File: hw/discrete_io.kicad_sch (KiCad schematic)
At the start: 32 parts, among them Q1 100V logic-level N-ch, Q2 100V logic-level N-ch

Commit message: Draw the connector; the power ground turns out to have no pin
Sheet 10 of 10. Not a circuit -- the harness boundary, and its job is to
be checkable against the machine: every pin the wiring diagram shows
wired to the net whichever sheet owns that signal already named, and
every pin it does not show left visibly empty.

41 of 94 pins wired, 53 left empty, every pin accounted for exactly once
in the netlist.

THE FINDING. GP3.8703.C4.pdf shows pin 21 as the battery positive feed
and shows no battery negative anywhere on the ECU connector. That is a
gap in the source rather than a contradiction in it -- the document is a
field troubleshooting diagram and its own scope note says it omits
"power grounds, unused pins and internal-only pins". It is still a gap
that stops a board: every other sheet in this project returns to GND,
the injector low sides carry 18 A into it, and at this boundary that net
has nowhere to go. It cannot be closed by choosing. Fifty pins have no
established function and several are certainly grounds -- a 94-way
connector feeding an 18 A injector stage does not have one return -- but
a wrong ground pin is not a rework, it is a harness that has to be
remade. Same for TRIP_LOOP, which is a NEW signal not on the OEM diagram
at all and needs one of the same fifty.

CONN_ECU_94 carries pin count and pin numbers, which are facts read off
page 4, and no footprint, because no part number is known. Pin names are
the diagram's own signal names where it shows the pin and blank where it
does not. Same treatment the op-amps and the comparator get.

Two distinctions the sheet makes explicit: pins 34 and 36 are SHARED
sensor returns and therefore signals, carried into difference amplifiers
on sensors_analog; pin 08 is rail pressure's dedicated return, with
nothing to reject, so it is simply ground here.

CROSS-SHEET AUDIT. 83 hierarchical net names across the ten sheets, 73
appearing on two or more. All ten that appear on only one sheet are
explained by an open it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
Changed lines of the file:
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@@
   )
   (hierarchical_label "RLY_MAIN" (shape input) (at 91.68 280.92 180)
-    (effects (font (size 1.27 1.27)) (justify left))
+    (effects (font (size 1.27 1.27)) (justify right))
   )
   (symbol (lib_id "Device:R") (at 101.84 296.92 0) (unit 1)
@@
   )
   (hierarchical_label "RLY_BUZZER" (shape input) (at 291.68 280.92 180)
-    (effects (font (size 1.27 1.27)) (justify left))
+    (effects (font (size 1.27 1.27)) (justify right))
   )
   (symbol (lib_id "Device:R") (at 301.84 296.92 0) (unit 1)

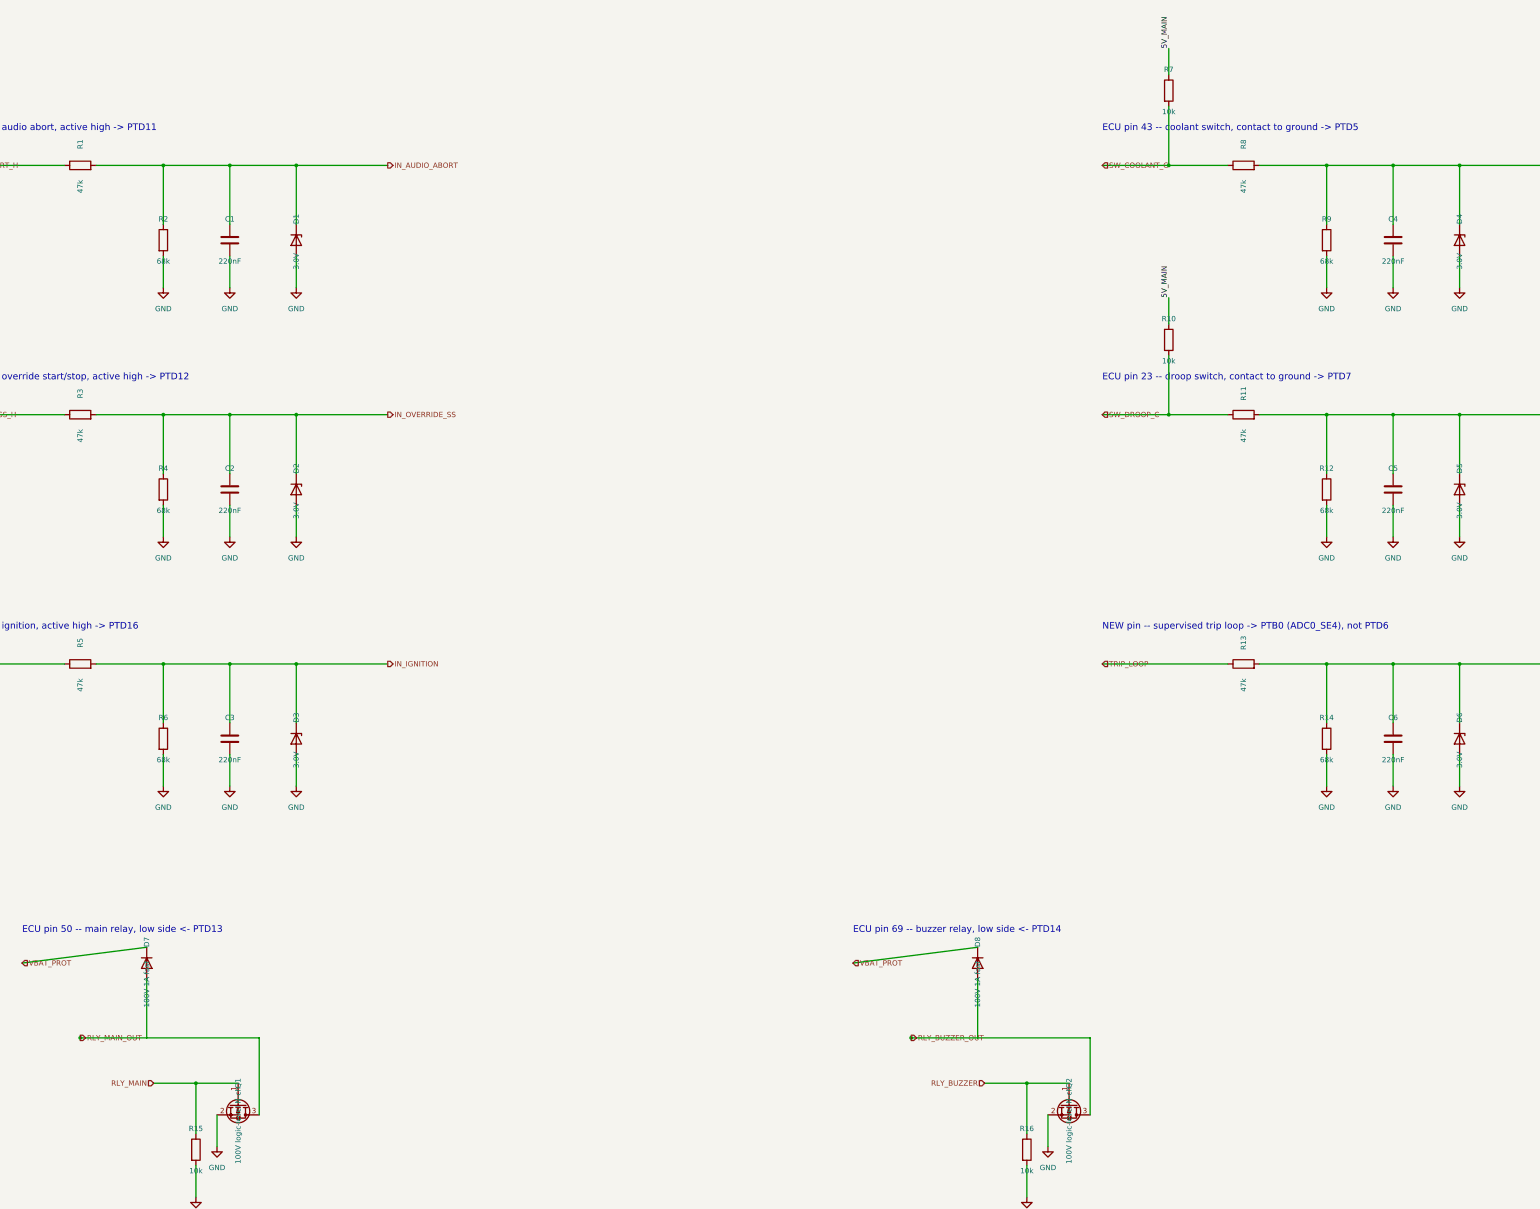
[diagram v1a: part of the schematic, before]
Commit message: Wire the root sheet: the project has a netlist for the first time
Ten sheets each passed their own netlist and the project had none. The
root sheet's ten sheet symbols carried NO hierarchical pins, so a net
name appearing on two sheets was two nets and nothing compared them --
the cross-sheet audit in the last commit was a name comparison, not a
connectivity check.

Each symbol now carries one pin per net its child exports, read OUT of
the child rather than declared in a second list that could drift: 162
pins across the ten, each with a stub and a label. Two labels with the
same name are one net, which is how 162 pins connect without routing
162 wires across a page nobody could read.

Exporting it found the other half of the same problem immediately.
kicad-cli reported annotation errors: every sheet generator allocated
R1, C1, U1 from its own counter, so ten sheets had ten parts called R1.
schlib.REF_BASE gives each sheet its own hundred -- KiCad's own
sheet-number x 100 convention, applied at generation time instead of by
a hand pass in Eeschema. 196 components, no duplicate reference.

hw/check_netlist.py is the gate, and the counterpart to sim/run_sim.py:
that one guards the component values, this one guards the connectivity.
Same rule -- an exemption is not a pass. Every single-pin net is listed
with its reason, and a net that STOPS being single-pin fails the check
until it is removed from the list. An open item that quietly closes is
as much a drift as one that quietly opens.

  196 components, every reference unique
  113 named nets carrying two or more pins
   18 named nets reaching one pin, each a recorded open item
      GND 134 pins, 3V3_MCU 27, VBAT_PROT 12 -- all spanning the project

The root sheet carries those eighteen on the page itself, grouped by
what they wait on, so a reader does not have to run a script to find
which ends are loose.

Full set plots to docs/pdf/ECU-Schematics.pdf, 11 pages.

Two rendering bugs fixed: sheet pin names and their stu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
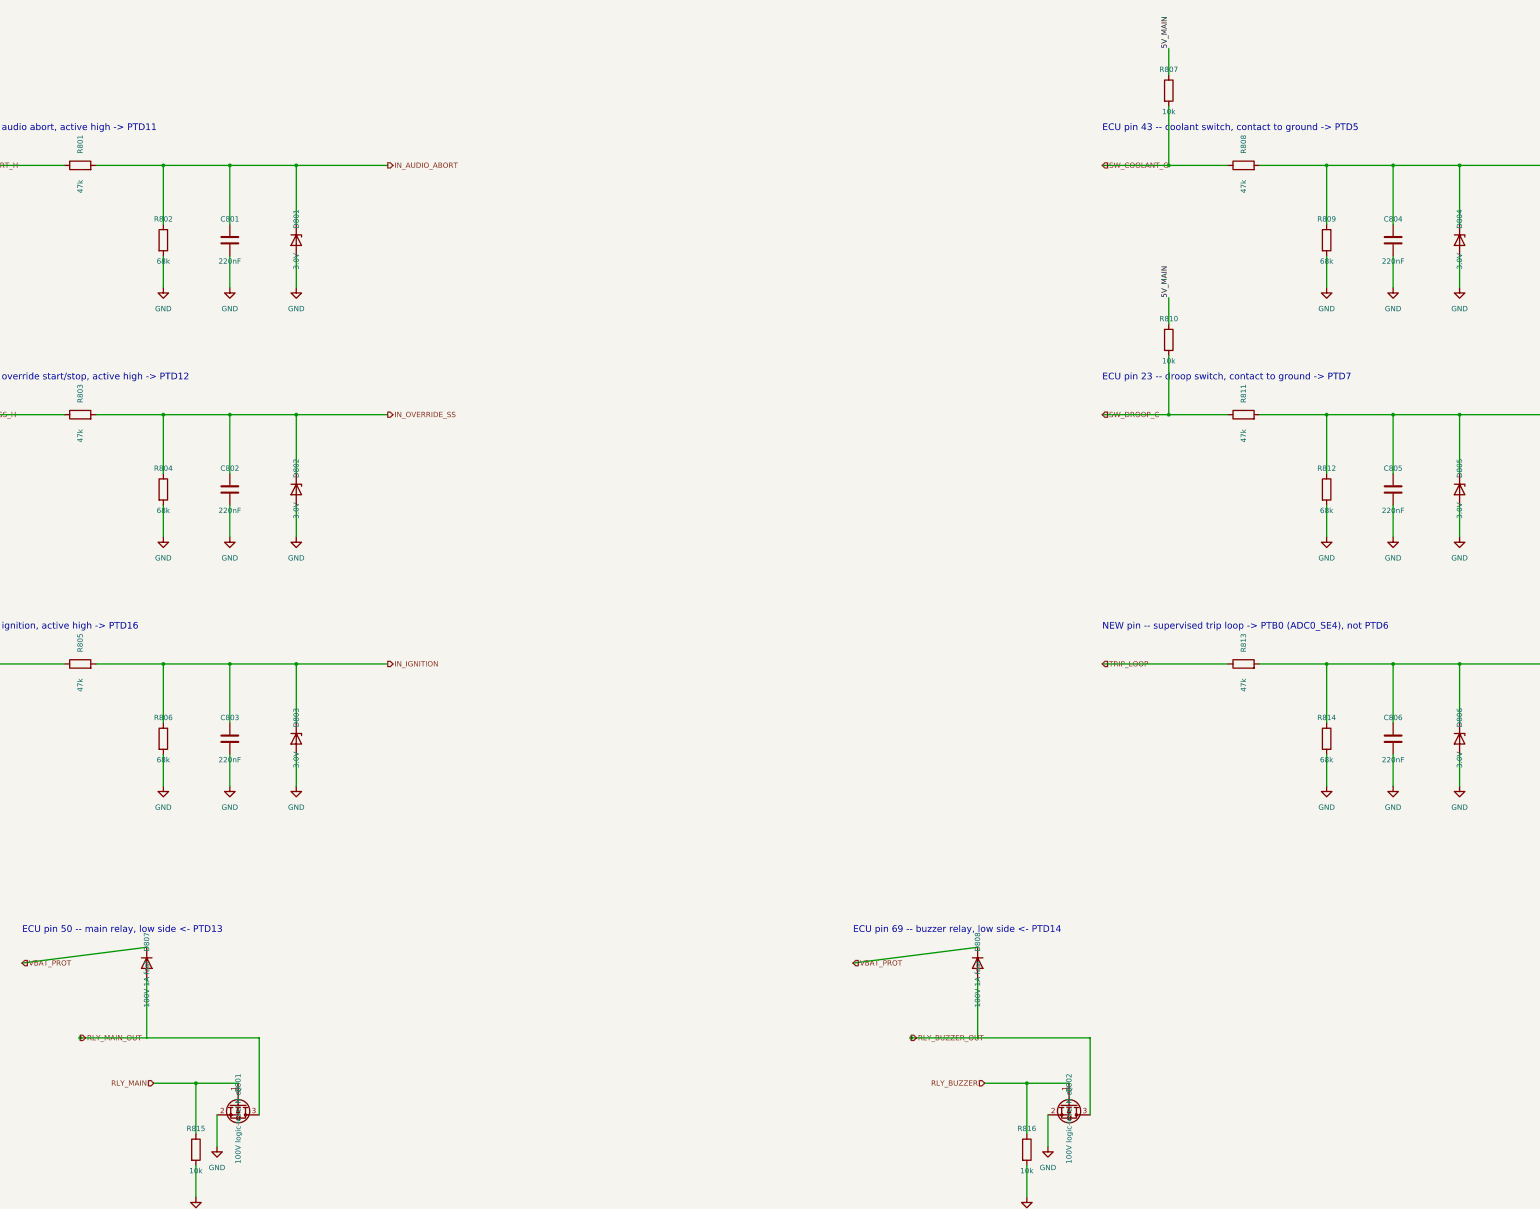
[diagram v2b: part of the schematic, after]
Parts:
- removed C1, C2, C3, C4, C5, C6: 220nF, symbol Device:C
- removed D1, D2, D3, D4, D5, D6: 3.0V, symbol Device:D_Zener
- removed D7, D8: 100V 1A fast, symbol Device:D
- removed Q1, Q2: 100V logic-level N-ch, symbol Device:Q_NMOS_GSD
- removed R1, R11, R13, R3, R5, R8: 47k, symbol Device:R
- removed R10, R15, R16, R7: 10k, symbol Device:R
- removed R12, R14, R2, R4, R6, R9: 68k, symbol Device:R
- added C801, C802, C803, C804, C805, C806: 220nF, symbol Device:C
- added D801, D802, D803, D804, D805, D806: 3.0V, symbol Device:D_Zener
- added D807, D808: 100V 1A fast, symbol Device:D
- added Q801, Q802: 100V logic-level N-ch, symbol Device:Q_NMOS_GSD
- added R801, R803, R805, R808, R811, R813: 47k, symbol Device:R
- added R802, R804, R806, R809, R812, R814: 68k, symbol Device:R
- added R807, R810, R815, R816: 10k, symbol Device:R
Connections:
- net 5V_MAIN: now also R807.1, R810.1
- net GND: now also C801.2, C802.2, C803.2, C804.2, C805.2, C806.2, D801.2 (A), D802.2 (A), D803.2 (A), D804.2 (A), D805.2 (A), D806.2 (A), Q801.2 (S), Q802.2 (S), R802.2, R804.2, R806.2, R809.2, R812.2, R814.2, R815.2, R816.2
- net IN_AUDIO_ABORT: now also C801.1, D801.1 (K), R801.2, R802.1
- net IN_AUDIO_ABORT_H: now also R801.1
- net IN_IGNITION: now also C803.1, D803.1 (K), R805.2, R806.1
- net IN_IGNITION_H: now also R805.1
- net IN_OVERRIDE_SS: now also C802.1, D802.1 (K), R803.2, R804.1
- net IN_OVERRIDE_SS_H: now also R803.1
- net RLY_BUZZER: now also Q802.1 (G), R816.1
- net RLY_BUZZER_OUT: now also D808.2 (A), Q802.3 (D)
- net RLY_MAIN: now also Q801.1 (G), R815.1
- net RLY_MAIN_OUT: now also D807.2 (A), Q801.3 (D)
- net SW_COOLANT: now also C804.1, D804.1 (K), R808.2, R809.1
- net SW_COOLANT_C: now also R807.2, R808.1
- net SW_DROOP: now also C805.1, D805.1 (K), R811.2, R812.1
- net SW_DROOP_C: now also R810.2, R811.1
- net TRIP_LOOP: now also R813.1
- net TRIP_SENSE: now also C806.1, D806.1 (K), R813.2, R814.1
- net VBAT_PROT: now also D807.1 (K), D808.1 (K)

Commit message: Check the project netlist, and fix the three things it caught
hw/check_netlist.py grew the two checks that found them, so neither can
come back quietly. It is the counterpart to sim/run_sim.py: that one
guards the component values, this one guards the connectivity.

5V_MAIN WAS FOUR NETS. The buck's 5 V output is a board rail -- both CAN
transceivers' VCC, the five difference amplifiers and the discrete
inputs' pull-ups run off it -- and it was a LOCAL label on every one of
those sheets. A local label stops at its sheet's edge, so three of the
four copies had no regulator on them. Each sheet's own netlist was
correct, which is exactly why ten clean per-sheet netlists never found
it. rails now exports it as a hierarchical label.

3V3_MCU WAS THREE. Same mechanism on can (both transceivers' VIO) and
speed_inputs, where the comparator's supply, both upper clamp diodes and
the bias divider sat on a five-pin net with no rail attached.

New check: any sheet-local net whose name shadows a project-wide net
name fails. That is the exact shape of both defects.

FIVE SUPPLY PINS HAD NO DECOUPLING CAPACITOR. The difference amplifiers
on sensors_analog were the only undecoupled supply pins on the board. No
simulation block was ever going to say so -- sensor_differential.cir
models an ideal amplifier with no supply pin at all. 100 nF each, at the
pin.

New check: walk every power_in pin in the project netlist and ask
whether a capacitor sits on the same net. 22 supply pins, all covered.
One documented exemption, the LM5164's BST pin, whose bootstrap
capacitor IS the net.

Gate now: 201 components with unique references, 108 named nets carrying
two or more pins, 18 reaching one and each a recorded open item, GND 139
pins, 3V3_MCU 36, 5V_MAIN 28, VBAT_PROT 12.

Schematic set re-plotted: docs/pdf/ECU-Schematics.pdf, 11 pages.
Suite still 24/24.

Co-Authored-By: Claude Opus 5 <noreply@anthropic.com>
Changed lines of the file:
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@@
     (stroke (width 0) (type default))
   )
-  (label "5V_MAIN" (at 336.0 31.84 90)
-    (effects (font (size 1.27 1.27)) (justify left bottom))
+  (hierarchical_label "5V_MAIN" (shape input) (at 336.0 31.84 90)
+    (effects (font (size 1.27 1.27)) (justify left))
   )
   (symbol (lib_id "Device:R") (at 354.0 60.0 90) (unit 1)
@@
     (stroke (width 0) (type default))
   )
-  (label "5V_MAIN" (at 336.0 91.84 90)
-    (effects (font (size 1.27 1.27)) (justify left bottom))
+  (hierarchical_label "5V_MAIN" (shape input) (at 336.0 91.84 90)
+    (effects (font (size 1.27 1.27)) (justify left))
   )
   (symbol (lib_id "Device:R") (at 354.0 120.0 90) (unit 1)
